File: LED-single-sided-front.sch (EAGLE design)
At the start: 33 parts, among them IC1 REG1117, IC2 REG1117, Q1 BUK98180-100A, Q2 BUK98180-100A, Q3 BUK98180-100A, Q4 BUK98180-100A, X1 53261-06

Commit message: A fresh start
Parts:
- removed B2: DBLS203G, rectifier:DBLS203G
- removed C1, C2, C4, C6: 0.1uF, SparkFun-Passives:CAP1206
- removed C5: 10uF, SparkFun-Capacitors:10UF-16V-10%(TANT)
- removed C7, C8: 10uF, SparkFun-Passives:CAP1206
- removed CN1: (no value), adafruit:JST_2PIN-THM
- removed IC1, IC2: REG1117, burr-brown:REG1117
- removed ICSP: 1X04_SMD_STRAIGHT_COMBO, SparkFun-Connectors:M04SMD_STRAIGHT_COMBO
- removed MPU: ESP8266_ESP-12, ESP8266-ESP12:ESP8266_ESP-12
- removed R10, R11, R12, R13: 10k, SparkFun-Resistors:RESISTOR1206
- removed U1: (no value), adafruit:PCA9685
- removed X1: 53261-06, con-molex:53261-06
- added H1, H2: MOUNT-HOLE3.0, holes:MOUNT-HOLE3.0
- added R2, R3, R4: 0, rcl:R-EU_0204/7
- added SV1, SV2: (no value), con-lstb:MA04-1
- R1: value (none) -> 0; device SparkFun-Resistors:RESISTOR1206 -> rcl:R-EU_0204/7
- R5, R6: value 1k -> 0; device SparkFun-Passives:RESISTOR1206 -> rcl:R-EU_0204/7
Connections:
- removed net #OE: R1.1, U1.#OE
- removed net 3.3V: C1.1, C2.1, C7.1, IC2.VOUT, MPU.VCC, R1.2, R10.1, R11.1, R12.1, R5.2, R6.2, U1.VDD
- removed net 5V: C4.1, C8.1, IC1.VOUT, IC2.VIN, ICSP.4
- removed net AC1: B2.AC1, CN1.2
- removed net AC2: B2.AC2, CN1.1
- removed net ADC: MPU.ADC
- removed net CH_PD: MPU.CH_PD, R11.2
- removed net GPIO0: MPU.GPIO0, R12.2, X1-4.S
- removed net GPIO12: MPU.GPIO12
- removed net GPIO13: MPU.GPIO13
- removed net GPIO14: MPU.GPIO14
- removed net GPIO15: MPU.GPIO15, R13.2
- removed net GPIO16: MPU.GPIO16
- removed net GPIO2: MPU.GPIO2
- removed net RESET: MPU.REST, R10.2, X1-3.S
- removed net RXD: ICSP.3, MPU.RXD, X1-1.S
- removed net SCL: MPU.GPIO5, R6.1, U1.SCL
- removed net SDA: MPU.GPIO4, R5.1, U1.SDA
- removed net TXD: ICSP.2, MPU.TXD, X1-2.S
- new net N$1: LED1.RED_C, R3.2
- new net N$2: LED1.GREEN_C, R2.2
- new net N$3: LED1.BLUE_C, R1.2
- new net N$4: LED3.RED_A, R4.1
- new net N$5: LED3.GREEN_A, R5.1
- new net N$6: LED3.BLUE_A, R6.1
- net 12V: now also SV1.4; no longer B2.+, C5.+, C6.1, IC1.VIN, X1-6.S
- net BLUE: now also SV1.3; no longer U1.PWM1
- net GND: now also SV2.1, SV2.2, SV2.3; no longer B2.-, C1.2, C2.2, C4.2, C5.-, C6.2, C7.2, C8.2, ICSP.1, MPU.GND, R13.1, U1.A0, U1.A1, U1.A2, U1.A3, U1.A4, U1.A5, U1.EXTCLK, U1.GND, X1-5.S
- net GREEN: now also SV1.1; no longer U1.PWM2
- net N$30: now also R4.2; no longer LED3.RED_A
- net N$31: now also R5.2; no longer LED3.GREEN_A
- net N$32: now also R6.2; no longer LED3.BLUE_A
- net N$33: now also R3.1; no longer LED1.RED_C
- net N$34: now also R2.1; no longer LED1.GREEN_C
- net N$35: now also R1.1; no longer LED1.BLUE_C
- net RED: now also SV1.2; no longer U1.PWM3
- net WHITE: now also SV2.4; no longer U1.PWM0
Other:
- note removed: "Diagnostic LEDs + Programming Port"
- note removed: "Microcontroller + PWM Generator + Pullups"
- note removed: "Power Rectification and Voltage Regulation"
- moved on the sheet: LED1, LED2, LED3, Q1, Q2, Q3, Q4, WL1, WL2, WL3

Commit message: mk9 brah.
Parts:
- R1, R2, R3, R4, R5, R6: device rcl:R-EU_0204/7 -> rcl:R-EU_R1206
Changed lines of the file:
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@@
 <part name="SV1" library="con-lstb" deviceset="MA04-1" device=""/>
 <part name="SV2" library="con-lstb" deviceset="MA04-1" device=""/>
-<part name="R1" library="rcl" deviceset="R-EU_" device="0204/7" value="0"/>
-<part name="R2" library="rcl" deviceset="R-EU_" device="0204/7" value="0"/>
-<part name="R3" library="rcl" deviceset="R-EU_" device="0204/7" value="0"/>
-<part name="R4" library="rcl" deviceset="R-EU_" device="0204/7" value="0"/>
-<part name="R5" library="rcl" deviceset="R-EU_" device="0204/7" value="0"/>
-<part name="R6" library="rcl" deviceset="R-EU_" device="0204/7" value="0"/>
+<part name="R1" library="rcl" deviceset="R-EU_" device="R1206" value="0"/>
+<part name="R2" library="rcl" deviceset="R-EU_" device="R1206" value="0"/>
+<part name="R3" library="rcl" deviceset="R-EU_" device="R1206" value="0"/>
+<part name="R4" library="rcl" deviceset="R-EU_" device="R1206" value="0"/>
+<part name="R5" library="rcl" deviceset="R-EU_" device="R1206" value="0"/>
+<part name="R6" library="rcl" deviceset="R-EU_" device="R1206" value="0"/>
 <part name="SUPPLY2" library="SparkFun-Aesthetics" deviceset="12V" device=""/>
 <part name="H1" library="holes" deviceset="MOUNT-HOLE" device="3.0"/>

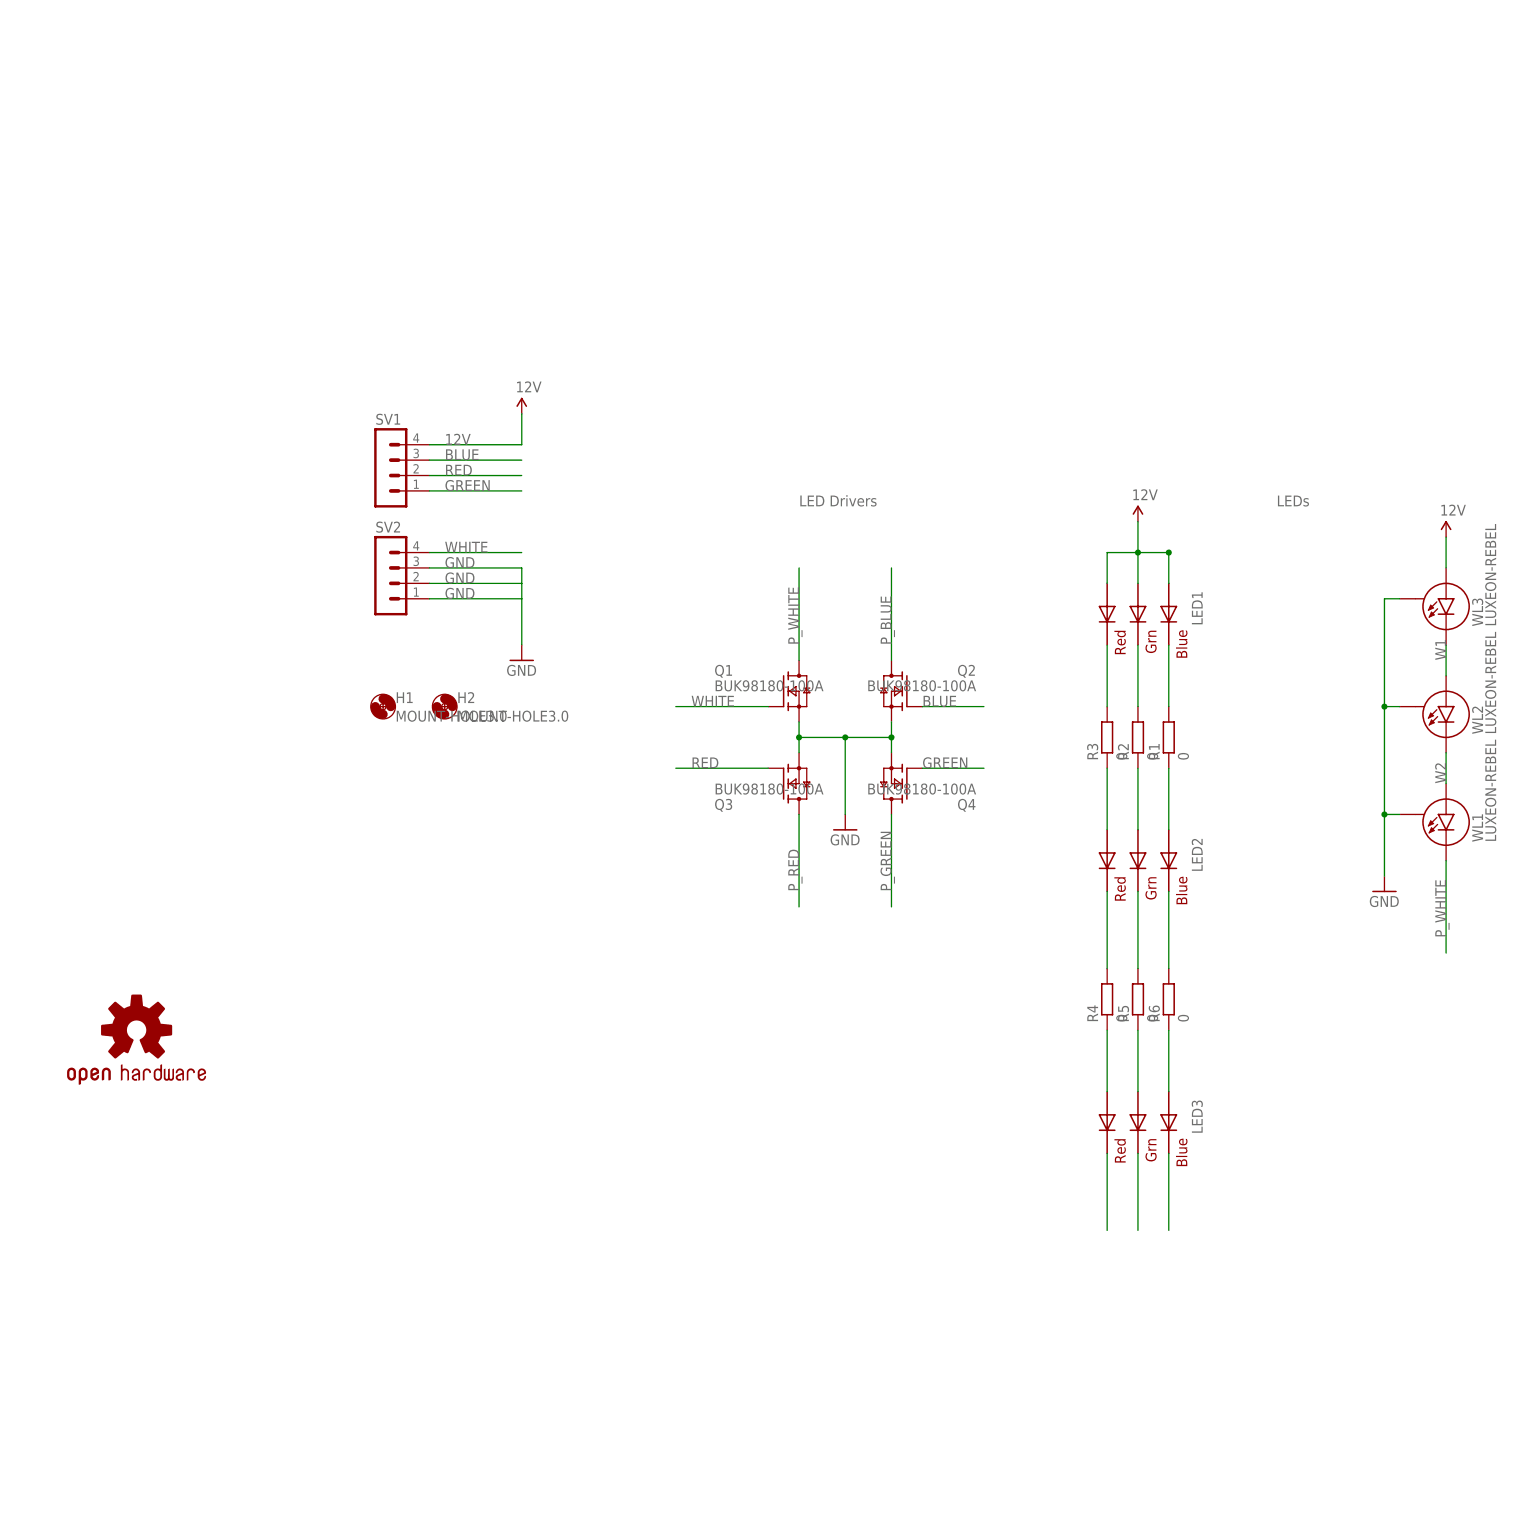
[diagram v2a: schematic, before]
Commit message: Put hole in middle of board (hurr durr donuts). Change to smaller mosfets. Add pulldown resistors.
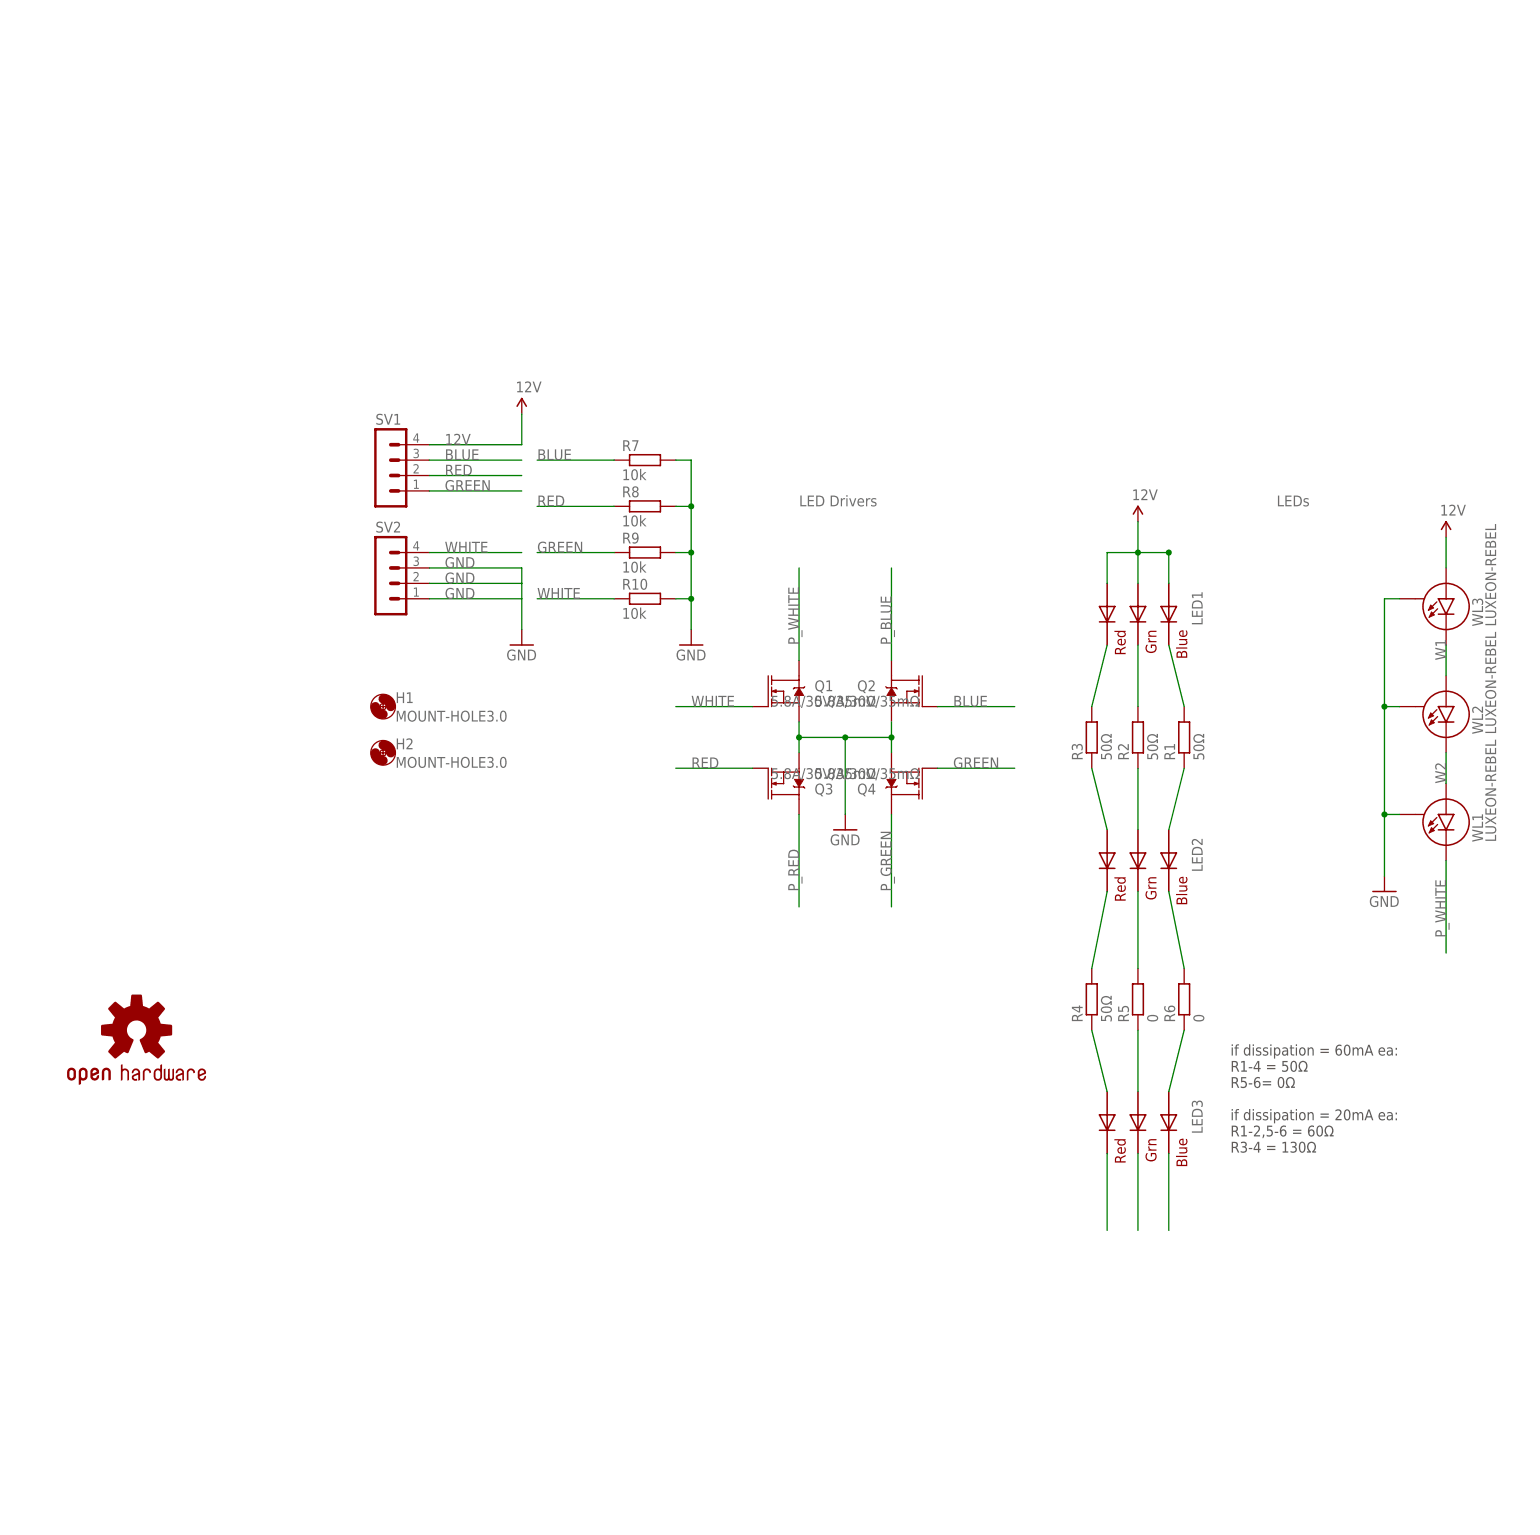
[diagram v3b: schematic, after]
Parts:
- added R10, R7, R8, R9: 10k, rcl:R-EU_R1206
- Q1, Q2, Q3, Q4: value BUK98180-100A -> 5.8A/30V/35mΩ; device nxp_60:BUK98180-100A -> SparkFun-DiscreteSemi:MOSFET-NCH-AO3404A
- R1, R2, R3, R4: value 0 -> 50Ω
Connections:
- net BLUE: now also R7.1
- net GND: now also R10.2, R7.2, R8.2, R9.2
- net GREEN: now also R9.1
- net RED: now also R8.1
- net WHITE: now also R10.1
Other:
- note added: "if dissipation = 60mA ea: R1-4 = 50Ω R5-6= 0Ω if dissipation = 20mA ea: R1-2,5-6 = 60Ω R3-4 = 130Ω"
- moved on the sheet: H2, R1, R3, R4, R6
